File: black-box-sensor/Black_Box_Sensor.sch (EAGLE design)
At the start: 52 parts, among them J1 104031-0811, J2 UX60-MB-5S8, J3 B4B-PH-SM4-TBT(LF)(SN), U1 ADXL375, U2 ADXL375, U3 ATMEGA32U4-AU, U4 FXAS21002CQR1, U5 MIC5504-3.3YM5-TR, U6 NL27WZ32USG, U8 AD8426ACPZ-WP

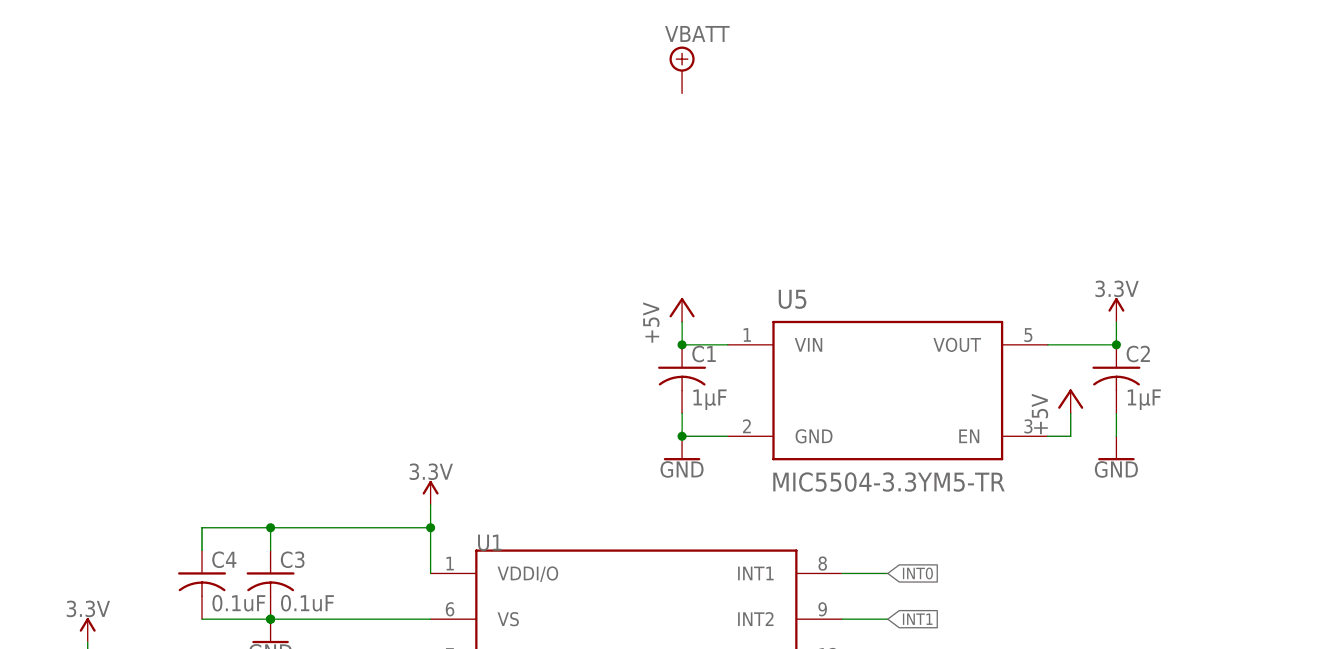
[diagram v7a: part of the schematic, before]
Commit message: add 5V regulator
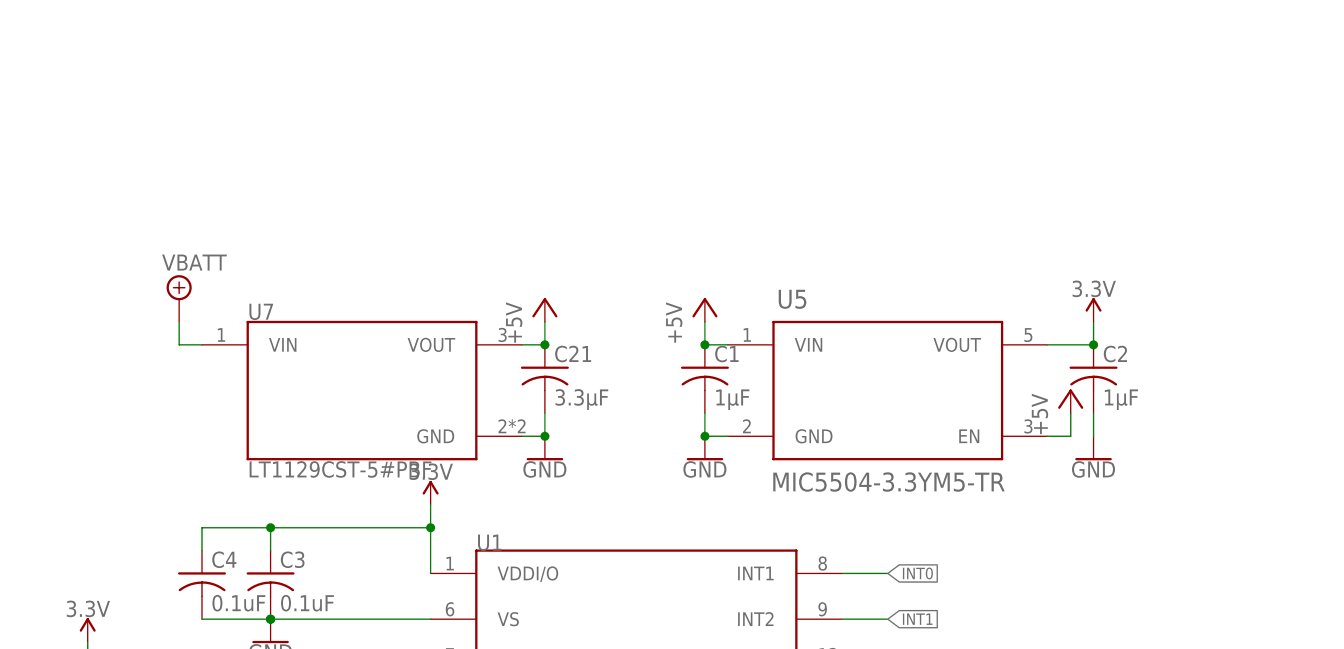
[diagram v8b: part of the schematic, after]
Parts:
- added C21: 3.3µF, rcl:C-USC0603
- added U7: LT1129CST-5#PBF, BBS_Library:LT1129CST-5#PBF
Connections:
- net +5V: now also C21.1, U7.VOUT
- net GND: now also C21.2, U7.GND
- net VBATT: now also U7.VIN
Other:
- moved on the sheet: C1, C2
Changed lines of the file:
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@@
 <part name="P+6" library="supply1" library_urn="urn:adsk.eagle:library:371" deviceset="+5V" device=""/>
 <part name="P+7" library="supply1" library_urn="urn:adsk.eagle:library:371" deviceset="+5V" device=""/>
+<part name="U7" library="BBS_Library" deviceset="LT1129CST-*#PBF" device="" technology="5"/>
+<part name="GND31" library="SparkFun-PowerSymbols" deviceset="GND" device=""/>
+<part name="C21" library="rcl" library_urn="urn:adsk.eagle:library:334" deviceset="C-US" device="C0603" package3d_urn="urn:adsk.eagle:package:23616/2" value="3.3µF">
+<spice>
+<pinmapping spiceprefix="C">
+<pinmap gate="G$1" pin="1" pinorder="1"/>
+<pinmap gate="G$1" pin="2" pinorder="2"/>
+</pinmapping>
+</spice>
+<attribute name="DKPN" value="CC0603KRX7R6BB105"/>
+<attribute name="VOLTAGE" value="10V"/>
+</part>
+<part name="P+8" library="supply1" library_urn="urn:adsk.eagle:library:371" deviceset="+5V" device=""/>
 </parts>
 <sheets>
@@
 <attribute name="VALUE" x="63.2206" y="100.5586" size="2.0828" layer="96" ratio="6" rot="SR0"/>
 </instance>
-<instance part="SUPPLY1" gate="G$1" x="53.34" y="147.32" smashed="yes">
-<attribute name="VALUE" x="51.435" y="150.495" size="1.778" layer="96"/>
-</instance>
-<instance part="GND1" gate="1" x="53.34" y="104.14" smashed="yes">
-<attribute name="VALUE" x="53.34" y="103.886" size="1.778" layer="96" align="top-center"/>
-</instance>
-<instance part="C1" gate="G$1" x="53.34" y="114.3" smashed="yes">
-<attribute name="NAME" x="54.356" y="114.935" size="1.778" layer="95"/>
-<attribute name="VALUE" x="54.356" y="110.109" size="1.778" layer="96"/>
-<attribute name="VOLTAGE" x="53.34" y="114.3" size="1.778" layer="96" display="off"/>
-<attribute name="DKPN" x="53.34" y="114.3" size="1.778" layer="96" display="off"/>
-</instance>
-<instance part="C2" gate="G$1" x="101.6" y="114.3" smashed="yes">
-<attribute name="NAME" x="102.616" y="114.935" size="1.778" layer="95"/>
-<attribute name="VALUE" x="102.616" y="110.109" size="1.778" layer="96"/>
-<attribute name="VOLTAGE" x="101.6" y="114.3" size="1.778" layer="96" display="off"/>
-<attribute name="DKPN" x="101.6" y="114.3" size="1.778" layer="96" display="off"/>
-</instance>
-<instance part="GND2" gate="1" x="101.6" y="104.14" smashed="yes">
-<attribute name="VALUE" x="101.6" y="103.886" size="1.778" layer="96" align="top-center"/>
+<instance part="SUPPLY1" gate="G$1" x="-2.54" y="121.92" smashed="yes">
+<attribute name="VALUE" x="-4.445" y="125.095" size="1.778" layer="96"/>
+</instance>
+<instance part="GND1" gate="1" x="55.88" y="104.14" smashed="yes">
+<attribute name="VALUE" x="55.88" y="103.886" size="1.778" layer="96" align="top-center"/>
+</instance>
+<instance part="C1" gate="G$1" x="55.88" y="114.3" smashed="yes">
+<attribute name="NAME" x="56.896" y="114.935" size="1.778" layer="95"/>
+<attribute name="VALUE" x="56.896" y="110.109" size="1.778" layer="96"/>
+<attribute name="VOLTAGE" x="55.88" y="114.3" size="1.778" layer="96" display="off"/>
+<attribute name="DKPN" x="55.88" y="114.3" size="1.778" layer="96" display="off"/>
+</instance>
+<instance part="C2" gate="G$1" x="99.06" y="114.3" smashed="yes">
+<attribute name="NAME" x="100.076" y="114.935" size="1.778" layer="95"/>
+<attribute name="VALUE" x="100.076" y="110.109" size="1.778" layer="96"/>
+<attribute name="VOLTAGE" x="99.06" y="114.3" size="1.778" layer="96" display="off"/>
+<attribute name="DKPN" x="99.06" y="114.3" size="1.778" layer="96" display="off"/>
+</instance>
+<instance part="GND2" gate="1" x="99.06" y="104.14" smashed="yes">
+<attribute name="VALUE" x="99.06" y="103.886" size="1.778" layer="96" align="top-center"/>
 </instance>
 <instance part="SUPPLY4" gate="G$1" x="25.4" y="99.06" smashed="yes">
@@
 <attribute name="VALUE" x="135.89" y="99.06" size="1.778" layer="96"/>
 </instance>
-<instance part="SUPPLY3" gate="G$1" x="101.6" y="119.38" smashed="yes">
-<attribute name="VALUE" x="101.6" y="122.174" size="1.778" layer="96" align="bottom-center"/>
+<instance part="SUPPLY3" gate="G$1" x="99.06" y="119.38" smashed="yes">
+<attribute name="VALUE" x="99.06" y="122.174" size="1.778" layer="96" align="bottom-center"/>
 </instance>
 <instance part="SUPPLY17" gate="G$1" x="132.08" y="111.76" smashed="yes">
@@
 <attribute name="VALUE" x="93.98" y="106.68" size="1.778" layer="96" rot="R90"/>
 </instance>
-<instance part="P+7" gate="1" x="53.34" y="121.92" smashed="yes">
-<attribute name="VALUE" x="50.8" y="116.84" size="1.778" layer="96" rot="R90"/>
+<instance part="P+7" gate="1" x="55.88" y="121.92" smashed="yes">
+<attribute name="VALUE" x="53.34" y="116.84" size="1.778" layer="96" rot="R90"/>
+</instance>
+<instance part="U7" gate="G$1" x="17.78" y="111.76" smashed="yes">
+<attribute name="NAME" x="5.08" y="119.634" size="1.778" layer="95" ratio="6" rot="SR0"/>
+<attribute name="VALUE" x="5.08" y="103.886" size="1.778" layer="96" ratio="6" rot="SR0" align="top-left"/>
+</instance>
+<instance part="GND31" gate="1" x="38.1" y="104.14" smashed="yes">
+<attribute name="VALUE" x="38.1" y="103.886" size="1.778" layer="96" align="top-center"/>
+</instance>
+<instance part="C21" gate="G$1" x="38.1" y="114.3" smashed="yes">
+<attribute name="NAME" x="39.116" y="114.935" size="1.778" layer="95"/>
+<attribute name="VALUE" x="39.116" y="110.109" size="1.778" layer="96"/>
+<attribute name="VOLTAGE" x="38.1" y="114.3" size="1.778" layer="96" display="off"/>
+<attribute name="DKPN" x="38.1" y="114.3" size="1.778" layer="96" display="off"/>
+</instance>
+<instance part="P+8" gate="1" x="38.1" y="121.92" smashed="yes">
+<attribute name="VALUE" x="35.56" y="116.84" size="1.778" layer="96" rot="R90"/>
 </instance>
 </instances>
@@
 <wire x1="139.7" y1="109.22" x2="132.08" y2="109.22" width="0.1524" layer="91"/>
 </segment>
+<segment>
+<pinref part="U7" gate="G$1" pin="VIN"/>
+<pinref part="SUPPLY1" gate="G$1" pin="VBATT"/>
+<wire x1="0" y1="116.84" x2="-2.54" y2="116.84" width="0.1524" layer="91"/>
+<wire x1="-2.54" y1="116.84" x2="-2.54" y2="119.38" width="0.1524" layer="91"/>
+</segment>
 </net>
 <net name="GND" class="0">
@@
 <pinref part="U5" gate="A" pin="GND"/>
 <pinref part="C1" gate="G$1" pin="2"/>
-<wire x1="53.34" y1="106.68" x2="58.42" y2="106.68" width="0.1524" layer="91"/>
-<wire x1="53.34" y1="109.22" x2="53.34" y2="106.68" width="0.1524" layer="91"/>
-<junction x="53.34" y="106.68"/>
+<wire x1="55.88" y1="106.68" x2="58.42" y2="106.68" width="0.1524" layer="91"/>
+<wire x1="55.88" y1="109.22" x2="55.88" y2="106.68" width="0.1524" layer="91"/>
+<junction x="55.88" y="106.68"/>
 </segment>
 <segment>
 <pinref part="GND2" gate="1" pin="GND"/>
 <pinref part="C2" gate="G$1" pin="2"/>
-<wire x1="101.6" y1="106.68" x2="101.6" y2="109.22" width="0.1524" layer="91"/>
+<wire x1="99.06" y1="106.68" x2="99.06" y2="109.22" width="0.1524" layer="91"/>
 </segment>
 <segment>
@@
 <wire x1="198.12" y1="104.14" x2="190.5" y2="104.14" width="0.1524" layer="91"/>
 </segment>
+<segment>
+<pinref part="U7" gate="G$1" pin="GND"/>
+<pinref part="GND31" gate="1" pin="GND"/>
+<wire x1="35.56" y1="106.68" x2="38.1" y2="106.68" width="0.1524" layer="91"/>
+<pinref part="C21" gate="G$1" pin="2"/>
+<wire x1="38.1" y1="109.22" x2="38.1" y2="106.68" width="0.1524" layer="91"/>
+<junction x="38.1" y="106.68"/>
+</segment>
 </net>
 <net name="3.3V" class="0">
@@
 <pinref part="U5" gate="A" pin="VOUT"/>
 <pinref part="C2" gate="G$1" pin="1"/>
-<wire x1="93.98" y1="116.84" x2="101.6" y2="116.84" width="0.1524" layer="91"/>
-<wire x1="101.6" y1="116.84" x2="101.6" y2="119.38" width="0.1524" layer="91"/>
-<junction x="101.6" y="116.84"/>
+<wire x1="93.98" y1="116.84" x2="99.06" y2="116.84" width="0.1524" layer="91"/>
+<wire x1="99.06" y1="116.84" x2="99.06" y2="119.38" width="0.1524" layer="91"/>
+<junction x="99.06" y="116.84"/>
 <pinref part="SUPPLY3" gate="G$1" pin="3.3V"/>
 </segment>
@@
 <pinref part="U5" gate="A" pin="VIN"/>
 <pinref part="C1" gate="G$1" pin="1"/>
-<wire x1="53.34" y1="116.84" x2="58.42" y2="116.84" width="0.1524" layer="91"/>
+<wire x1="55.88" y1="116.84" x2="58.42" y2="116.84" width="0.1524" layer="91"/>
 <pinref part="P+7" gate="1" pin="+5V"/>
-<wire x1="53.34" y1="119.38" x2="53.34" y2="116.84" width="0.1524" layer="91"/>
-<junction x="53.34" y="116.84"/>
+<wire x1="55.88" y1="119.38" x2="55.88" y2="116.84" width="0.1524" layer="91"/>
+<junction x="55.88" y="116.84"/>
 </segment>
 <segment>
@@
 <wire x1="96.52" y1="109.22" x2="96.52" y2="106.68" width="0.1524" layer="91"/>
 </segment>
-</net>
+<segment>
+<pinref part="P+8" gate="1" pin="+5V"/>
+<pinref part="C21" gate="G$1" pin="1"/>
+<wire x1="38.1" y1="119.38" x2="38.1" y2="116.84" width="0.1524" layer="91"/>
+<pinref part="U7" gate="G$1" pin="VOUT"/>
+<wire x1="35.56" y1="116.84" x2="38.1" y2="116.84" width="0.1524" layer="91"/>
+<junction x="38.1" y="116.84"/>
+</segment>
+</net>
